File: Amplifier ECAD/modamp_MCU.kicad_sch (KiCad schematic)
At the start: 1 part, among them U4 Teensy 4.1

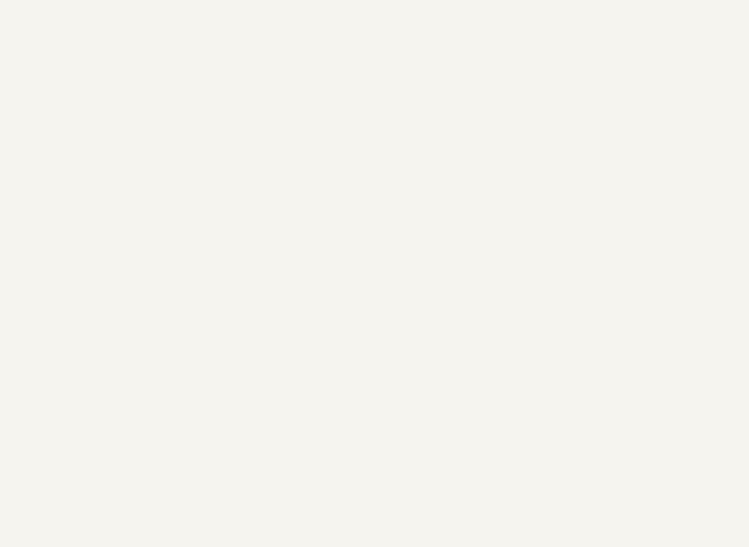
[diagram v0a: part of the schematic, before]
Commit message: File renaming; updating supplier references
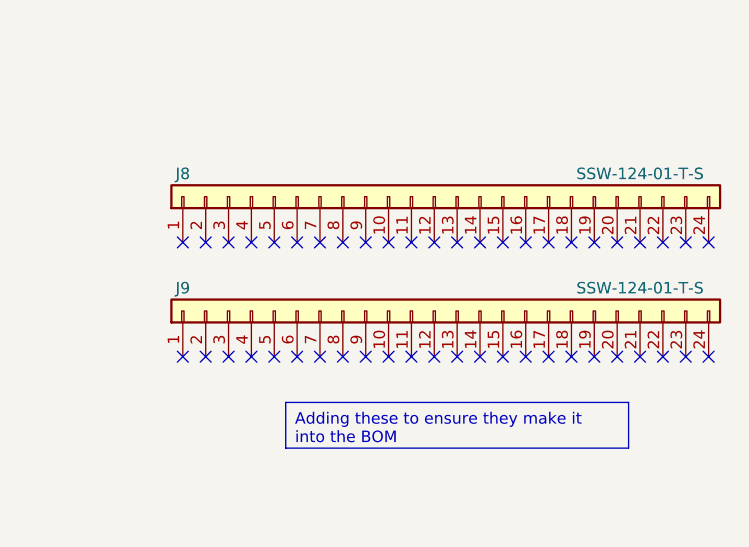
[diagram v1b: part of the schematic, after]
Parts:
- added J8, J9: SSW-124-01-T-S, Connector_PinSocket_2.54mm:PinSocket_1x24_P2.54mm_Vertical, symbol Custom-Connector:SSW-124-01-T-S
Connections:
- no-connect marks 0 -> 48
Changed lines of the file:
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@@
     (company "Ishaan Govindarajan")
   )
+  (no_connect (at 259.08 115.57))
+  (no_connect (at 226.06 115.57))
+  (no_connect (at 233.68 115.57))
+  (no_connect (at 254 115.57))
+  (no_connect (at 231.14 128.27))
+  (no_connect (at 261.62 128.27))
+  (no_connect (at 210.82 128.27))
+  (no_connect (at 251.46 115.57))
+  (no_connect (at 233.68 128.27))
+  (no_connect (at 208.28 115.57))
+  (no_connect (at 266.7 128.27))
+  (no_connect (at 256.54 115.57))
+  (no_connect (at 215.9 128.27))
+  (no_connect (at 259.08 128.27))
+  (no_connect (at 243.84 115.57))
+  (no_connect (at 246.38 128.27))
+  (no_connect (at 210.82 115.57))
+  (no_connect (at 243.84 128.27))
+  (no_connect (at 246.38 115.57))
+  (no_connect (at 213.36 115.57))
+  (no_connect (at 228.6 128.27))
+  (no_connect (at 208.28 128.27))
+  (no_connect (at 220.98 115.57))
+  (no_connect (at 264.16 128.27))
+  (no_connect (at 236.22 115.57))
+  (no_connect (at 238.76 115.57))
+  (no_connect (at 236.22 128.27))
+  (no_connect (at 261.62 115.57))
+  (no_connect (at 256.54 128.27))
+  (no_connect (at 254 128.27))
+  (no_connect (at 241.3 128.27))
+  (no_connect (at 248.92 128.27))
+  (no_connect (at 266.7 115.57))
+  (no_connect (at 226.06 128.27))
+  (no_connect (at 215.9 115.57))
+  (no_connect (at 264.16 115.57))
+  (no_connect (at 223.52 115.57))
+  (no_connect (at 220.98 128.27))
+  (no_connect (at 213.36 128.27))
+  (no_connect (at 218.44 115.57))
+  (no_connect (at 231.14 115.57))
+  (no_connect (at 223.52 128.27))
+  (no_connect (at 238.76 128.27))
+  (no_connect (at 251.46 128.27))
+  (no_connect (at 248.92 115.57))
+  (no_connect (at 241.3 115.57))
+  (no_connect (at 228.6 115.57))
+  (no_connect (at 218.44 128.27))
   (wire (pts (xy 90.17 142.24) (xy 96.52 142.24))
     (stroke (width 0) (type default))
@@
     (effects (font (size 1.27 1.27) (color 255 255 255 1)) (justify left top))
   )
+  (text_box "Adding these to ensure they make it into the BOM"
+    (at 219.71 133.35 0) (size 38.1 5.08)
+    (stroke (width 0) (type default) (color 0 0 72 1))
+    (fill (type color) (color 0 0 132 1))
+    (effects (font (size 1.27 1.27) (color 255 255 255 1)) (justify left top))
+  )
   (hierarchical_label "LED_R2" (shape output) (at 80.01 77.47 180) (fields_autoplaced)
     (effects (font (size 1.27 1.27)) (justify right))
@@
     (pin "33")
     (instances
-      (project "Amplifier Hardware R1"
+      (project "Amplifier Hardware RevB"
         (path "/e2090ed5-0c0e-40bb-b0f5-d128ffed01ae/cceb7d38-e430-415a-965f-3fe96e0b8929"
           (reference "U4") (unit 2)
@@
     )
   )
+  (symbol (lib_id "Custom-Connector:SSW-124-01-T-S") (at 236.22 110.49 90) (unit 1)
+    (in_bom yes) (on_board no) (dnp no)
+    (property "Reference" "J8" (at 208.28 107.95 90)
+      (effects (font (size 1.27 1.27)))
+    )
+    (property "Value" "SSW-124-01-T-S" (at 259.08 107.95 90)
+      (effects (font (size 1.27 1.27)))
+    )
+    (property "Footprint" "Connector_PinSocket_2.54mm:PinSocket_1x24_P2.54mm_Vertical" (at 236.22 110.49 0)
+      (effects (font (size 1.27 1.27)) hide)
+    )
+    (property "Datasheet" "http://suddendocs.samtec.com/prints/ssw-s.pdf" (at 236.22 110.49 0)
+      (effects (font (size 1.27 1.27)) hide)
+    )
+    (property "Manufacturer" "Samtec Inc." (at 236.22 110.49 0)
+      (effects (font (size 1.27 1.27)) hide)
+    )
+    (property "Part Number" "SSW-124-01-T-S" (at 236.22 110.49 0)
+      (effects (font (size 1.27 1.27)) hide)
+    )
+    (pin "1")
+    (pin "10")
+    (pin "11")
+    (pin "12")
+    (pin "13")
+    (pin "14")
+    (pin "15")
+    (pin "16")
+    (pin "17")
+    (pin "18")
+    (pin "19")
+    (pin "2")
+    (pin "20")
+    (pin "21")
+    (pin "22")
+    (pin "23")
+    (pin "24")
+    (pin "3")
+    (pin "4")
+    (pin "5")
+    (pin "6")
+    (pin "7")
+    (pin "8")
+    (pin "9")
+    (instances
+      (project "Amplifier Hardware RevB"
+        (path "/e2090ed5-0c0e-40bb-b0f5-d128ffed01ae/cceb7d38-e430-415a-965f-3fe96e0b8929"
+          (reference "J8") (unit 1)
+        )
+      )
+    )
+  )
+  (symbol (lib_id "Custom-Connector:SSW-124-01-T-S") (at 236.22 123.19 90) (unit 1)
+    (in_bom yes) (on_board no) (dnp no)
+    (property "Reference" "J9" (at 208.28 120.65 90)
+      (effects (font (size 1.27 1.27)))
+    )
+    (property "Value" "SSW-124-01-T-S" (at 259.08 120.65 90)
+      (effects (font (size 1.27 1.27)))
+    )
+    (property "Footprint" "Connector_PinSocket_2.54mm:PinSocket_1x24_P2.54mm_Vertical" (at 236.22 123.19 0)
+      (effects (font (size 1.27 1.27)) hide)
+    )
+    (property "Datasheet" "http://suddendocs.samtec.com/prints/ssw-s.pdf" (at 236.22 123.19 0)
+      (effects (font (size 1.27 1.27)) hide)
+    )
+    (property "Manufacturer" "Samtec Inc." (at 236.22 123.19 0)
+      (effects (font (size 1.27 1.27)) hide)
+    )
+    (property "Part Number" "SSW-124-01-T-S" (at 236.22 123.19 0)
+      (effects (font (size 1.27 1.27)) hide)
+    )
+    (pin "1")
+    (pin "10")
+    (pin "11")
+    (pin "12")
+    (pin "13")
+    (pin "14")
+    (pin "15")
+    (pin "16")
+    (pin "17")
+    (pin "18")
+    (pin "19")
+    (pin "2")
+    (pin "20")
+    (pin "21")
+    (pin "22")
+    (pin "23")
+    (pin "24")
+    (pin "3")
+    (pin "4")
+    (pin "5")
+    (pin "6")
+    (pin "7")
+    (pin "8")
+    (pin "9")
+    (instances
+      (project "Amplifier Hardware RevB"
+        (path "/e2090ed5-0c0e-40bb-b0f5-d128ffed01ae/cceb7d38-e430-415a-965f-3fe96e0b8929"
+          (reference "J9") (unit 1)
+        )
+      )
+    )
+  )
   (symbol (lib_id "Daughterboards:Teensy_4_1_Basic") (at 116.84 132.08 0) (unit 3)
     (in_bom yes) (on_board yes) (dnp no)
@@
     (pin "33")
     (instances
-      (project "Amplifier Hardware R1"
+      (project "Amplifier Hardware RevB"
         (path "/e2090ed5-0c0e-40bb-b0f5-d128ffed01ae/cceb7d38-e430-415a-965f-3fe96e0b8929"
           (reference "U4") (unit 3)
